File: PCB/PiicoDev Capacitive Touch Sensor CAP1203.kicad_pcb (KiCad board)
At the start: 2 copper layers, 25.4 x 52 mm, 44 parts, among them J1 , J11 Conn_01x01_Male, J12 Conn_01x01_Male, J13 Conn_01x01_Male, J2 , J3 Conn_PiicoDev_header_01x04_Ma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, J4 Conn_01x01_Male, J5 Conn_01x01_Male, J6 Conn_01x01_Male, J7 Conn_01x01_Male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

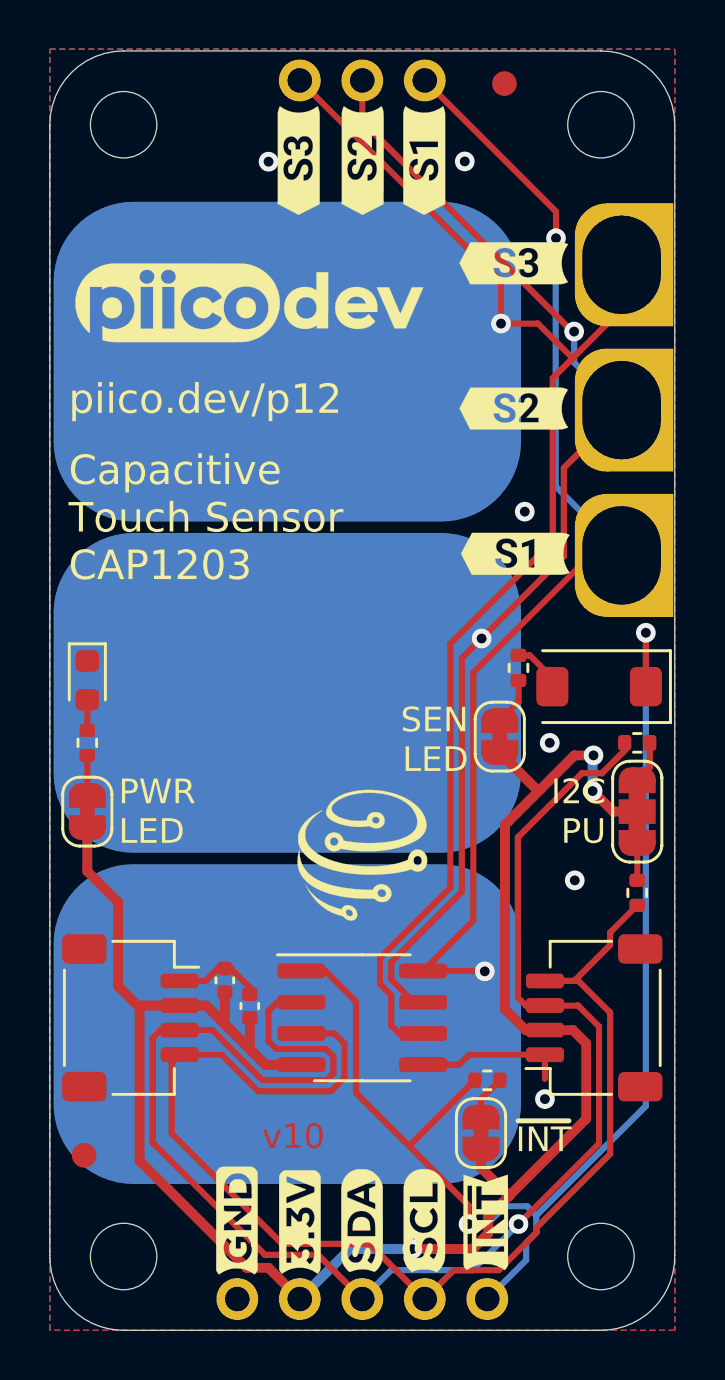
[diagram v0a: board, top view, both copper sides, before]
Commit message: Upgrade to KiCad 6.0.5
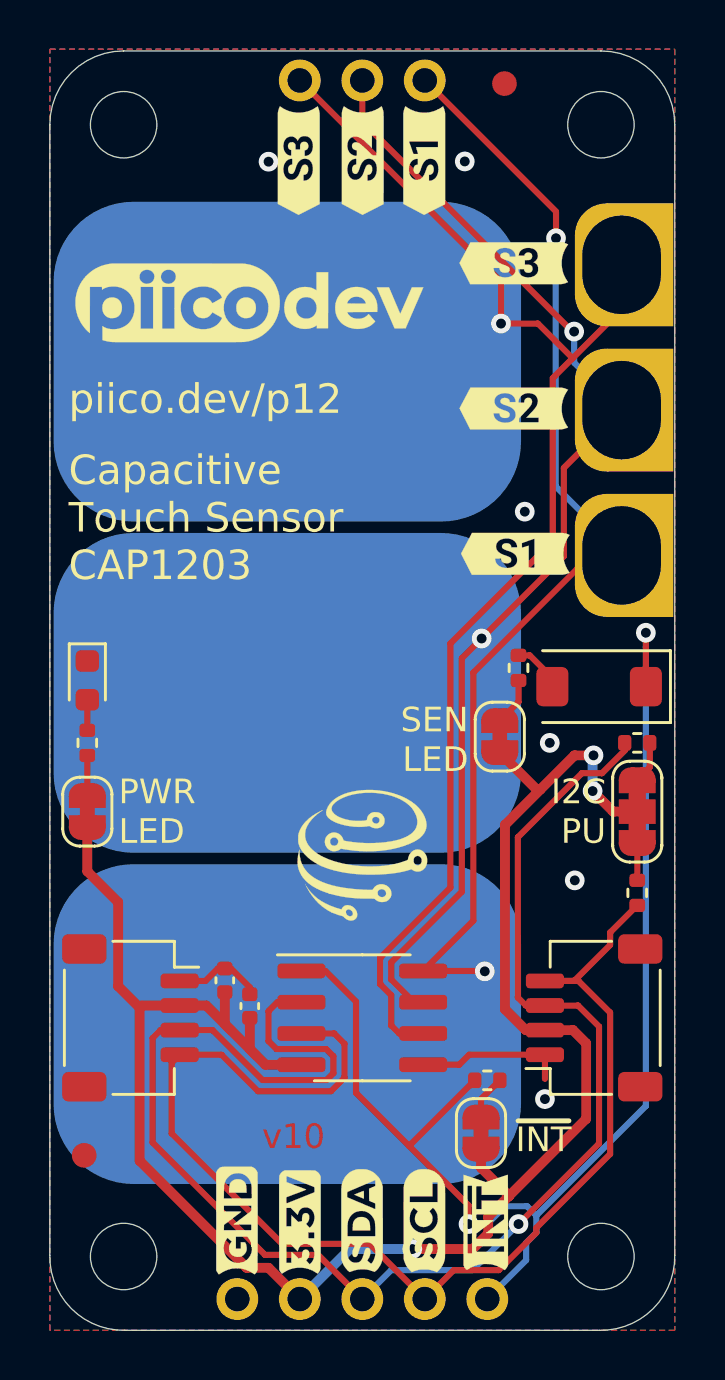
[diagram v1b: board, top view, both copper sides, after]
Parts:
- JP4: value ~INT -> ~{INT}
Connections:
- net /~INT renamed /~{INT}
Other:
- net class Default removed
- net class Power removed
- board text added: "Designed at Core Electronics by Peter Johnston"
- board text added: "~{INT}"
- board text removed: "Designed at Core Electronics"
- board text removed: "~INT"
